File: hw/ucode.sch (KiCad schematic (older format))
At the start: 13 parts

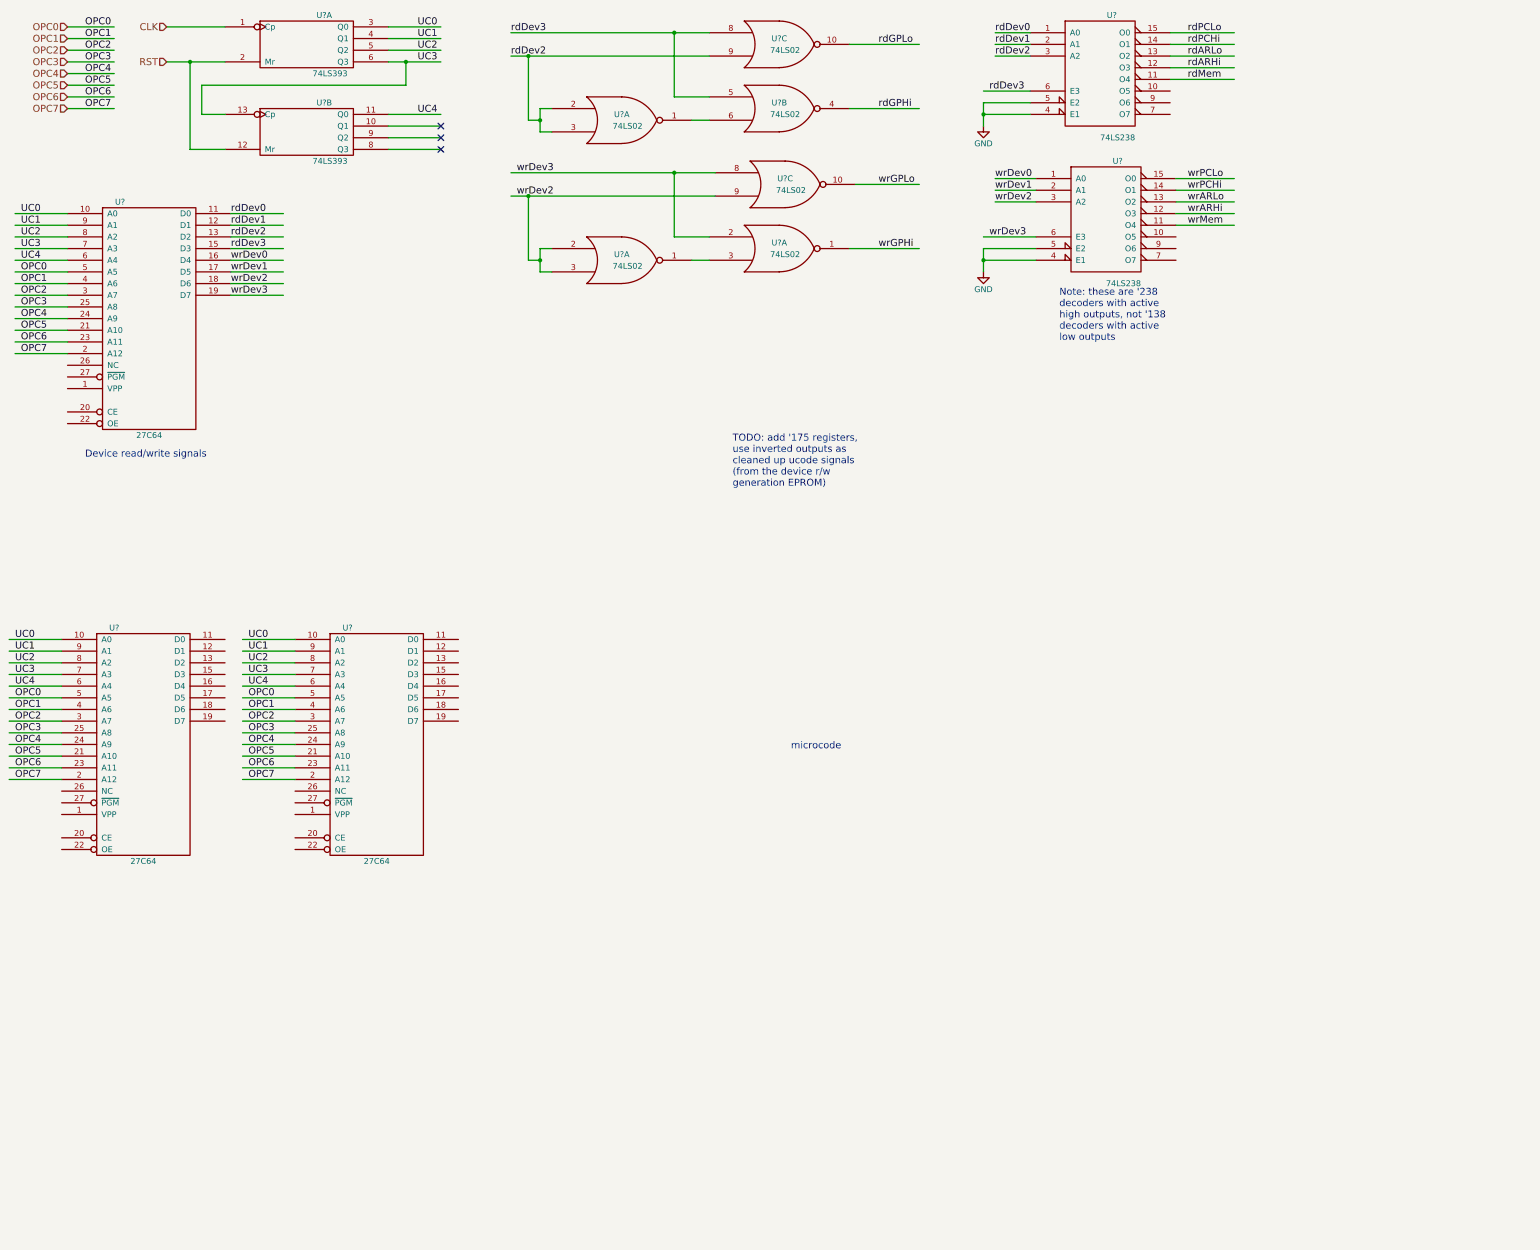
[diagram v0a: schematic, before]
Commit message: annotated more components
Also some more work on connecting modules together
and adding glue logic.
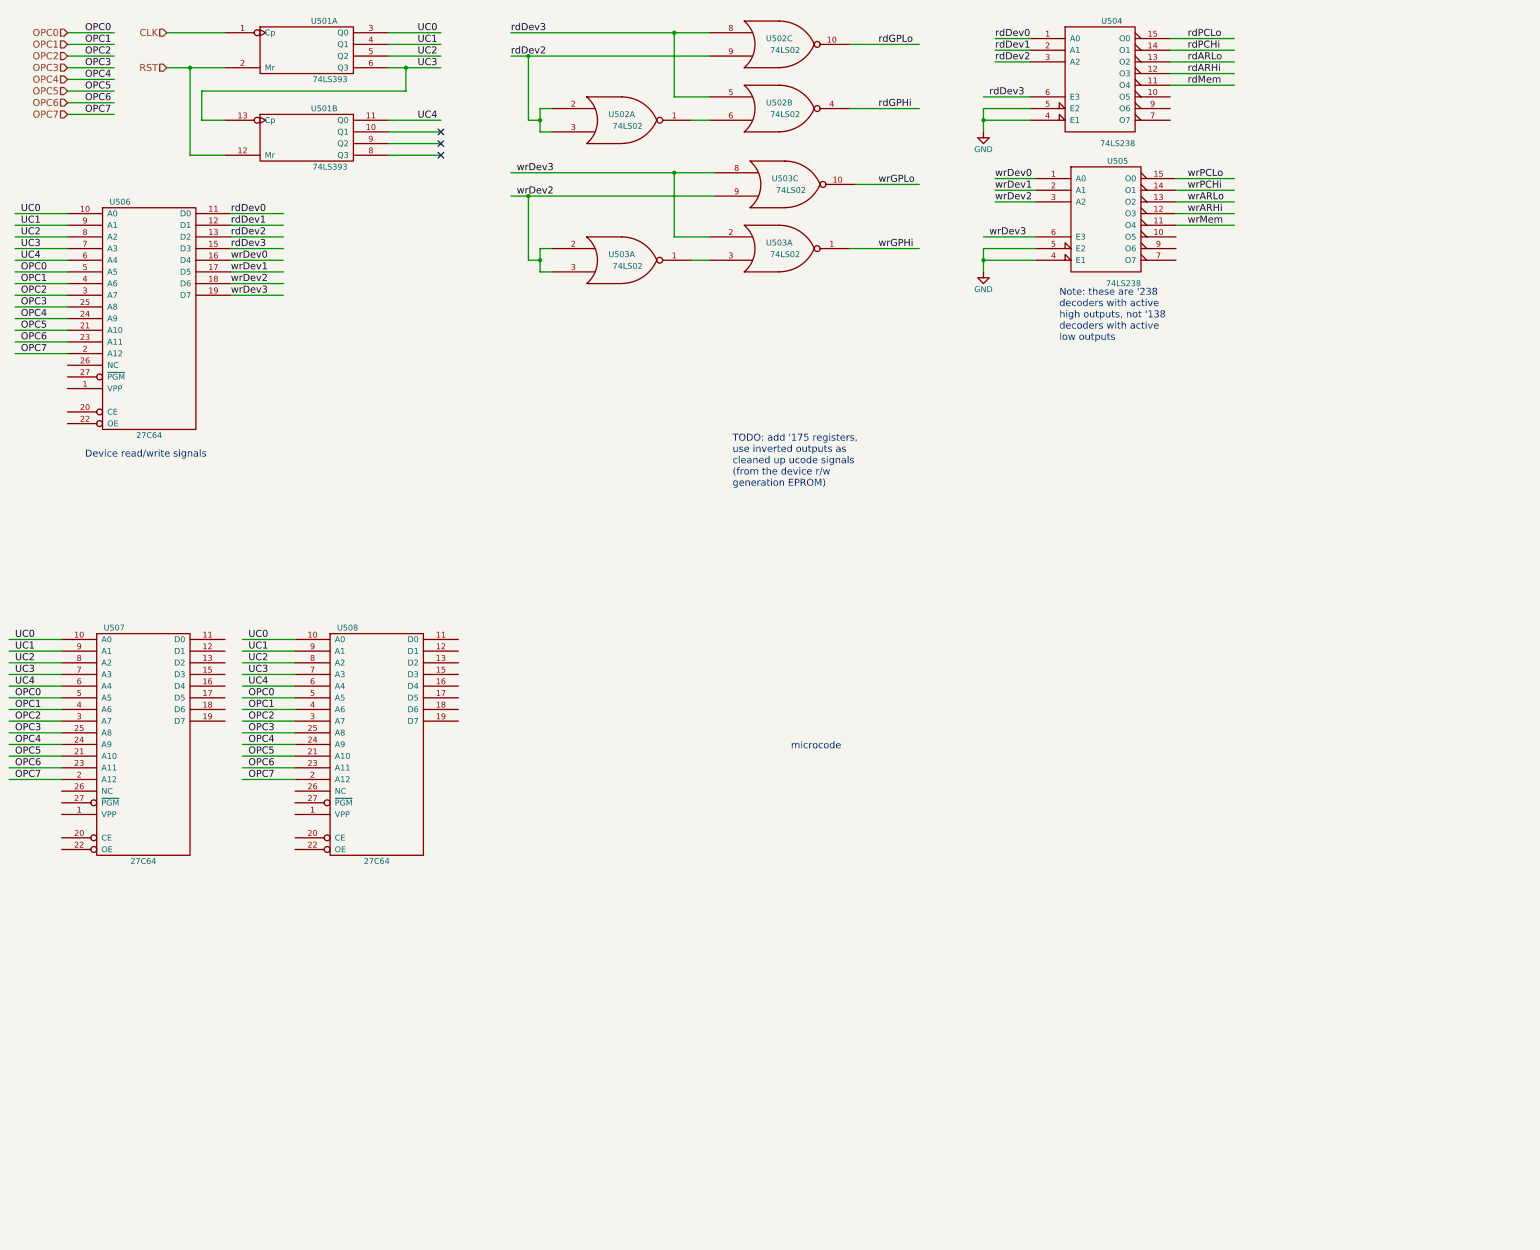
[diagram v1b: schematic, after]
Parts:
- gave numbers to parts that had none: 8
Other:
- moved on the sheet: U501A, U501B, U504

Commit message: added ucode output registers
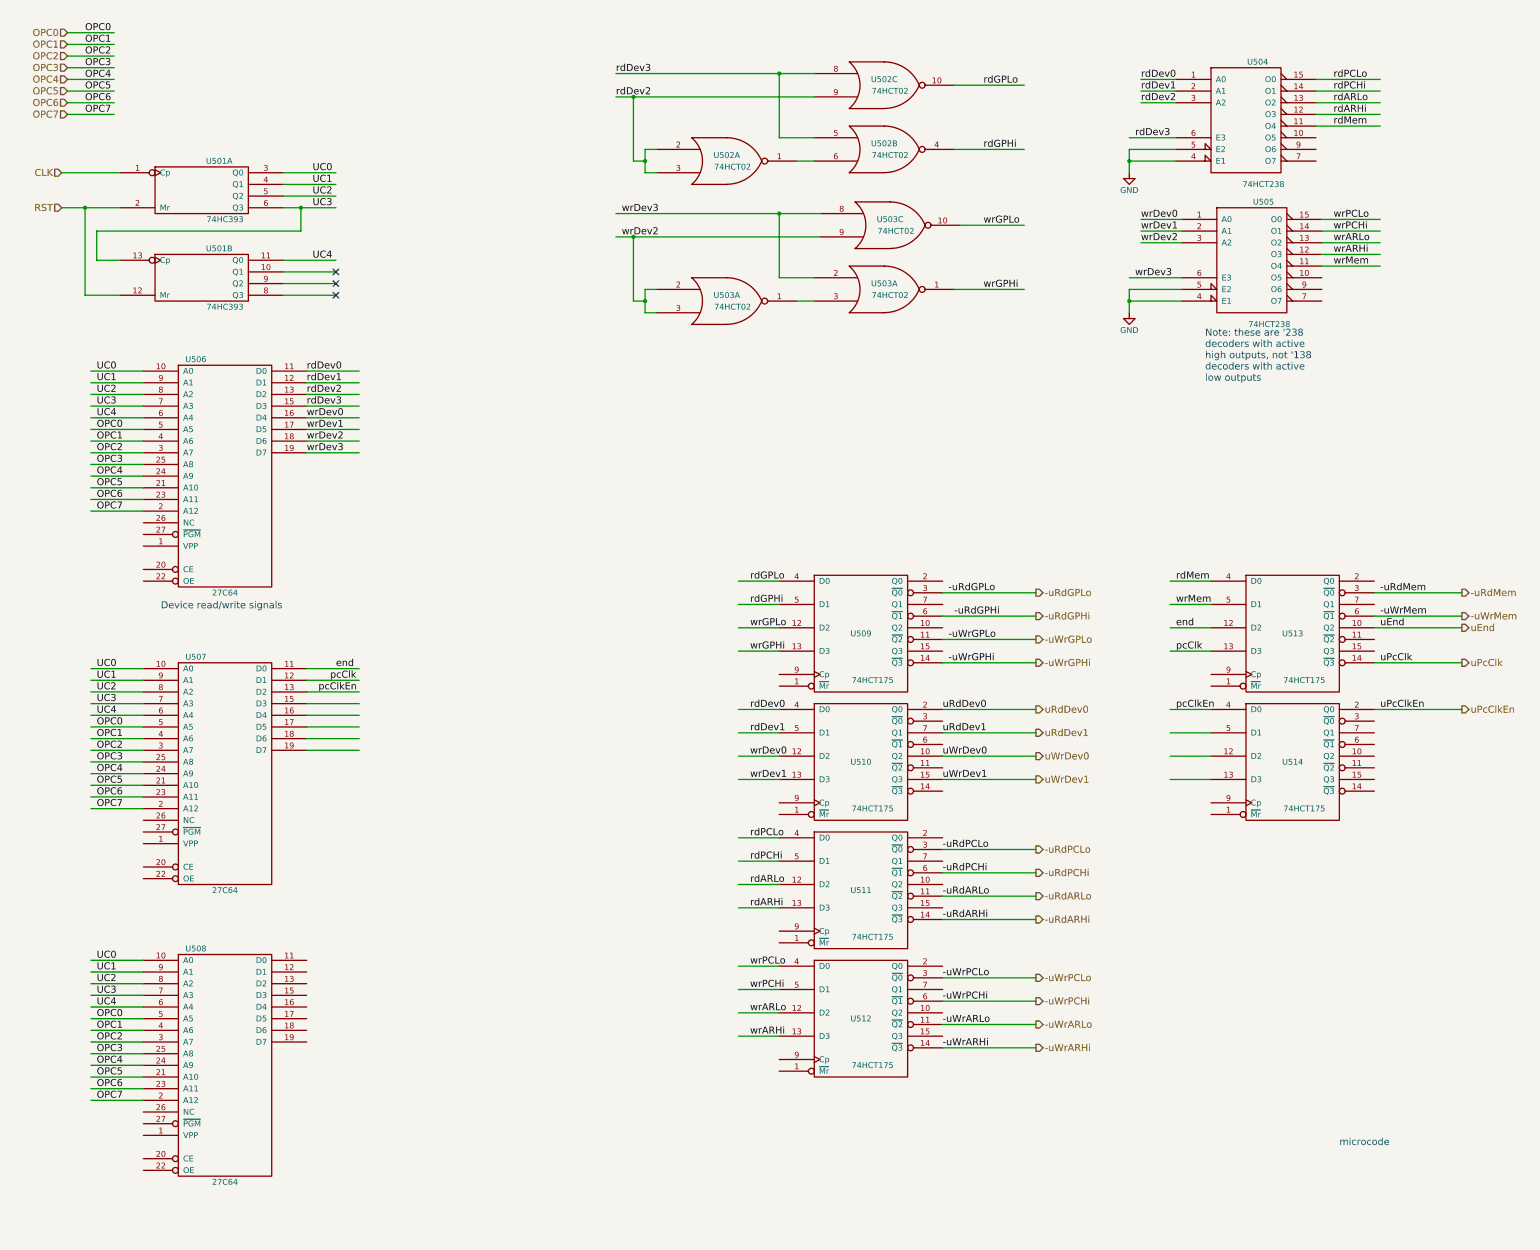
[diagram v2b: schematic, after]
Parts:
- added U509, U510, U511, U512, U513, U514: 74HCT175, symbol 74LS175
- U501: value 74LS393 -> 74HC393
- U502, U503: value 74LS02 -> 74HCT02
- U504, U505: value 74LS238 -> 74HCT238
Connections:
- net labels added: -uRdARHi, -uRdARLo, -uRdGPHi, -uRdGPLo, -uRdMem, -uRdPCHi, -uRdPCLo, -uWrARHi, -uWrARLo, -uWrGPHi, -uWrGPLo, -uWrMem, -uWrPCHi, -uWrPCLo, end, pcClk, pcClkEn, uEnd, uPcClk, uPcClkEn, uRdDev0, uRdDev1, uWrDev0, uWrDev1
- wire segments 119 -> 172
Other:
- note removed: "TODO: add '175 registers,\nuse inverted outputs as\ncleaned up ucode signals\n(from the device r/w\ngeneration EPROM)"
- moved on the sheet: U501A, U501B, U502A, U502B, U502C, U503A, U503C, U504, U505, U506, U507, U508

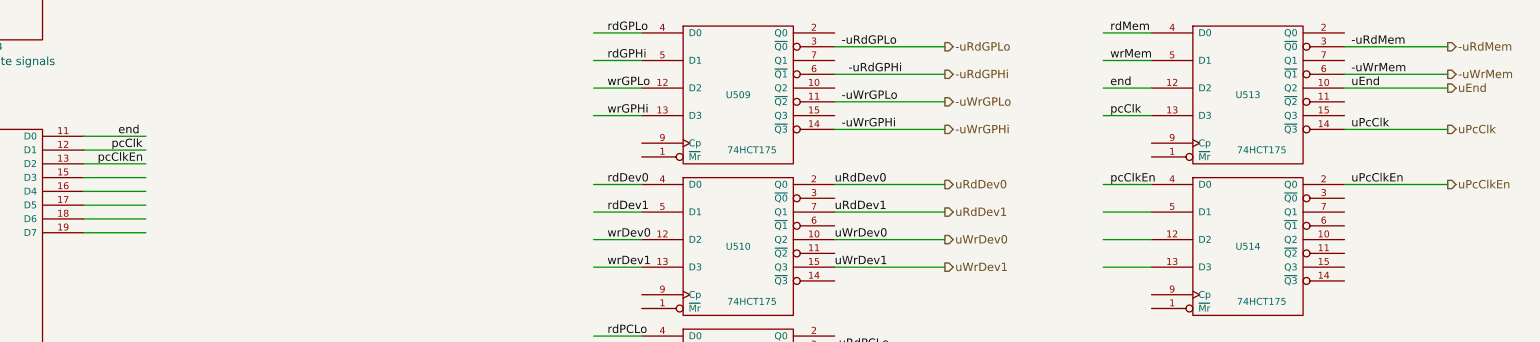
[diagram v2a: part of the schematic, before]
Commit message: eliminated pcClkEn signal
There's no need to selectively enable/disable
the count function in the PC because the PC
clock signal (pcClk) is generated explicitly
by the microcode, and clock pulses are sent
only when we actually want to increment the PC
value.

This allowed a simplicification of the carry
logic, and eliminated the need for the 74HC30
in the last stage of the carry logic.
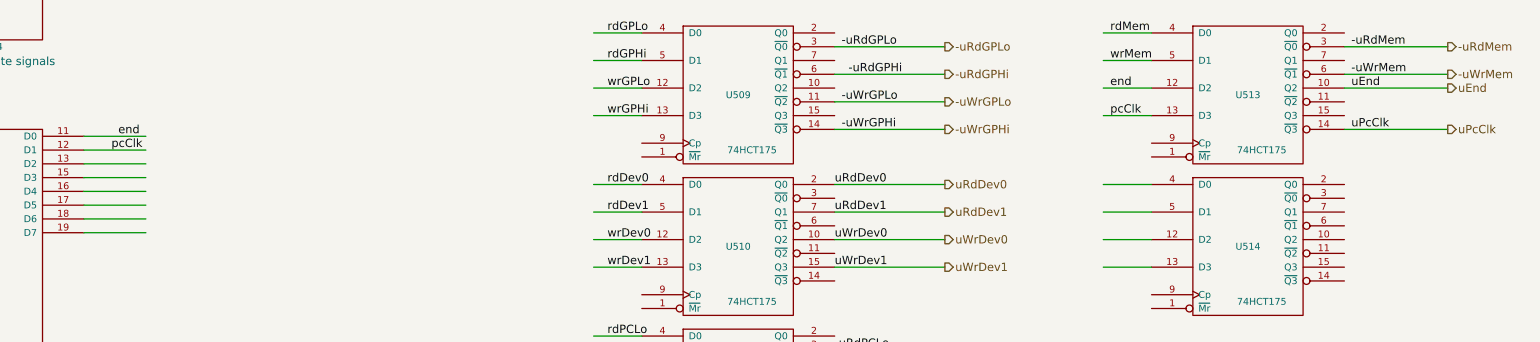
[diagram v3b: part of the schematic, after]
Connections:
- net labels removed: pcClkEn, uPcClkEn
- wire segments 172 -> 171
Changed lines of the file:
@@
 Text Label 3300 6200 0    60   ~ 0
 pcClk
-Text Label 3200 6300 0    60   ~ 0
-pcClkEn
 $Comp
 L 74LS175 U509
@@
 Text Label 10550 5950 0    60   ~ 0
 pcClk
-Text Label 10550 6450 0    60   ~ 0
-pcClkEn
 Text Label 12300 6050 0    60   ~ 0
 uPcClk
-Text Label 12300 6450 0    60   ~ 0
-uPcClkEn
 Text HLabel 9350 5450 2    60   Output ~ 0
 -uRdGPLo
@@
 	3100 6200 3550 6200
 Wire Wire Line
-	3100 6300 3550 6300
-Wire Wire Line
 	3100 6400 3550 6400
 Wire Wire Line
@@
 	12250 5750 13000 5750
 Wire Wire Line
-	10850 6450 10500 6450
-Wire Wire Line
 	10850 6650 10500 6650
 Wire Wire Line
@@
 Wire Wire Line
 	12250 6050 13000 6050
-Wire Wire Line
-	12250 6450 13000 6450
 Text HLabel 13000 5450 2    60   Output ~ 0
 -uRdMem
@@
 Text HLabel 13000 6050 2    60   Output ~ 0
 uPcClk
-Text HLabel 13000 6450 2    60   Output ~ 0
-uPcClkEn
+Wire Wire Line
+	3100 6300 3550 6300
+Wire Wire Line
+	10850 6450 10500 6450
 $EndSCHEMATC
